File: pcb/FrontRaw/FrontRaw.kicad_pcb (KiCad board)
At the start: 2 copper layers, 54.5 x 106.4 mm, 11 parts

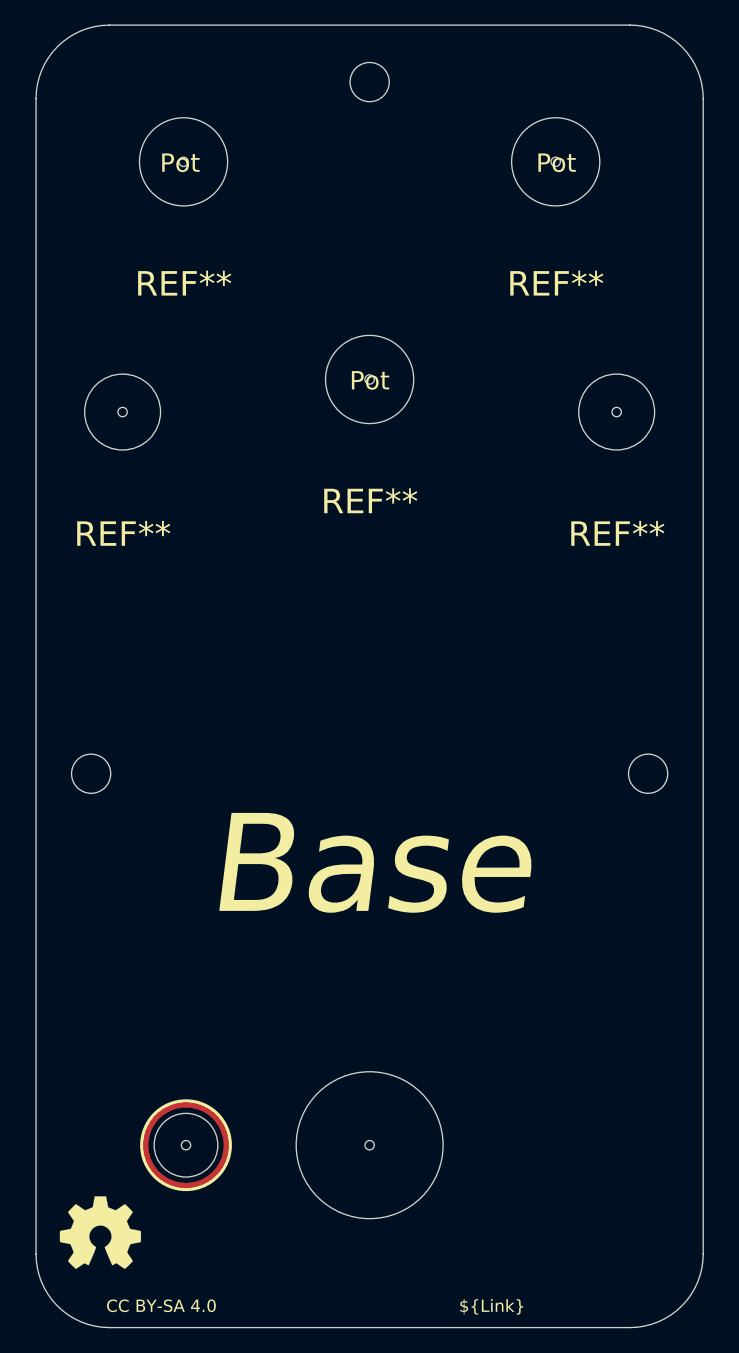
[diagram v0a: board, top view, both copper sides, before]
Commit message: [FrontRaw] Continue graphical design on frontpanel
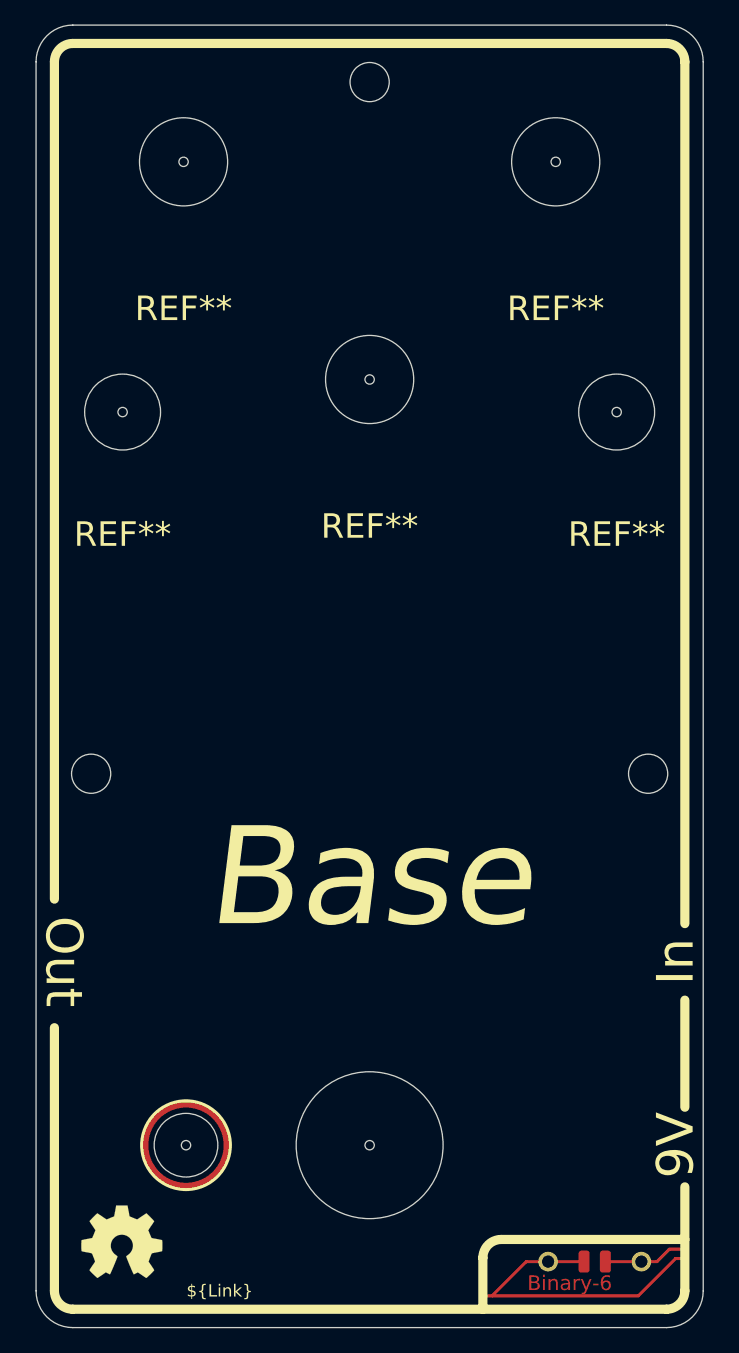
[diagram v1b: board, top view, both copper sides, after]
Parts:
- added H7: Symbol_Binary6, MeineBib:Binary_6_v0.1_tiny_silk, F.Cu at (167.9, 160.5)
- added MK6: PentThin, MeineBib:PentThin, B.Cu at (149.5, 73.4)
- moved REF** 1.90 mm to (129.2, 157.9)
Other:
- outline, holes or cut-outs redrawn
- board text added: "9V"
- board text added: "In"
- board text added: "Out"
- board text removed: "CC BY-SA 4.0"
- board text removed: "Pot"

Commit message: [FrontRaw] Add copper zones and keepout
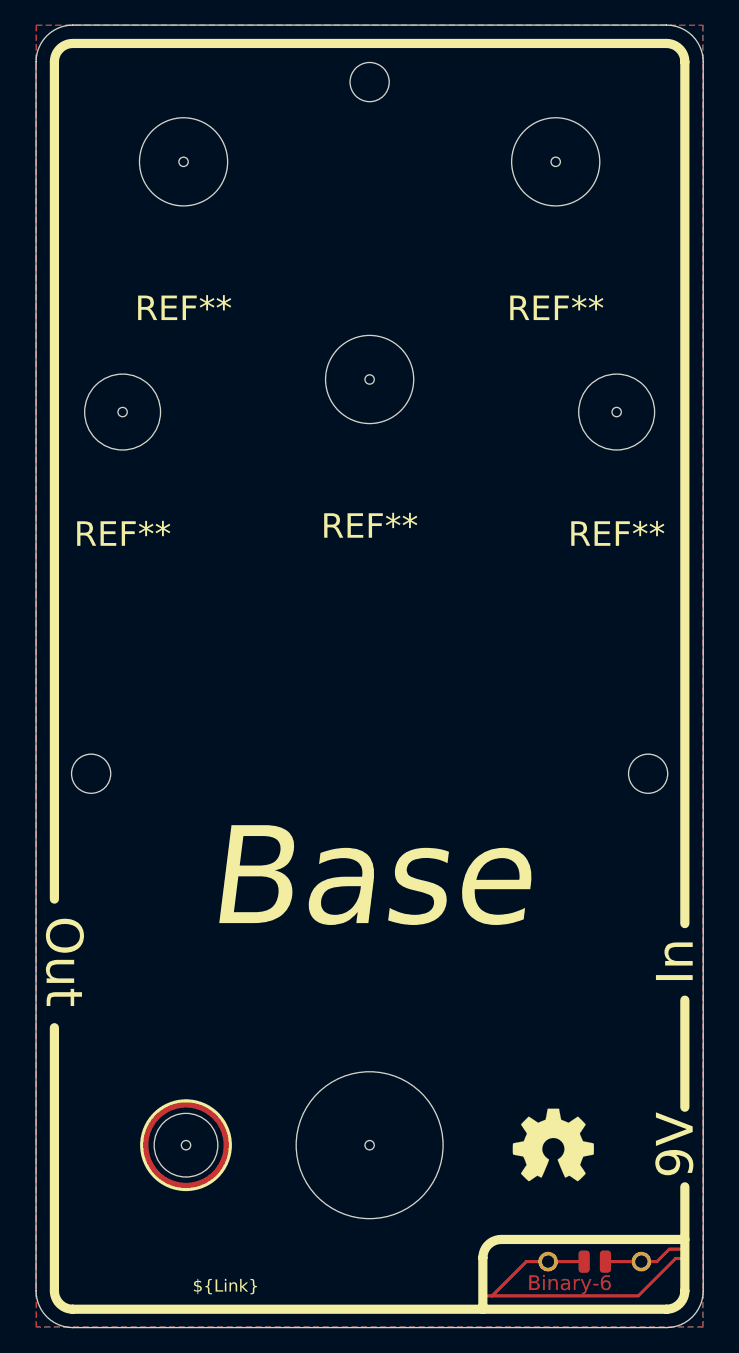
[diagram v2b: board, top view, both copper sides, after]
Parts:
- moved REF** 36.1 mm to (164.5, 150.0)
- moved MK6 0.61 mm to (149.5, 72.8)
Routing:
- added copper zone on B.Cu, net (none)
- added copper zone on F.Cu, net (none)
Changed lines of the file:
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@@
     (solder_mask_min_width 0.254)
     (aux_axis_origin 149.5 63.13)
-    (grid_origin 175.25 161.875)
+    (grid_origin 125.25 58.475)
     (pcbplotparams
       (layerselection 0x0001020_7ffffffe)
@@
   )
   (footprint "Symbol:OSHW-Symbol_6.7x6mm_SilkScreen" (layer "F.Cu")
-    (at 129.25 157.875)
+    (at 164.5 149.975)
     (descr "Open Source Hardware Symbol")
     (tags "Logo Symbol OSHW")
@@
       (effects (font (size 1 1) (thickness 0.15)))
     )
-    (pad "" np_thru_hole circle (at 0 0) (size 7.2 7.2) (drill 7.2) (layers *.Mask))
     (pad "" np_thru_hole circle (at 0 0) (size 14 14) (drill 0.762) (layers *.Mask))
+    (pad "" np_thru_hole circle (at 0 0) (size 7.2 7.2) (drill 7.2) (layers *.Mask)
+      (clearance 3.6))
   )
   (footprint "MeineBib:EigenesMountingHole_3.2mm_M3_Small" (layer "F.Cu")
@@
       (effects (font (size 1 1) (thickness 0.15)))
     )
-    (pad "" np_thru_hole circle (at 0 0) (size 6.2 6.2) (drill 6.2) (layers *.Mask))
     (pad "" np_thru_hole circle (at 0 0) (size 12 12) (drill 0.762) (layers *.Mask))
+    (pad "" np_thru_hole circle (at 0 0) (size 6.2 6.2) (drill 6.2) (layers *.Mask)
+      (clearance 3.1))
   )
   (footprint "MeineBib:Drill_ToggleSwitch_6,2mm" (layer "F.Cu")
@@
       (effects (font (size 1 1) (thickness 0.15)))
     )
-    (pad "" np_thru_hole circle (at 0 0) (size 6.2 6.2) (drill 6.2) (layers *.Mask))
     (pad "" np_thru_hole circle (at 0 0) (size 12 12) (drill 0.762) (layers *.Mask))
+    (pad "" np_thru_hole circle (at 0 0) (size 6.2 6.2) (drill 6.2) (layers *.Mask)
+      (clearance 3.1))
   )
   (footprint "MeineBib:Drill_9mmPot_7,2mm" (layer "F.Cu")
@@
       (effects (font (size 1 1) (thickness 0.15)))
     )
-    (pad "" np_thru_hole circle (at 0 0) (size 7.2 7.2) (drill 7.2) (layers *.Mask))
+    (pad "" np_thru_hole circle (at 0 0) (size 7.2 7.2) (drill 7.2) (layers *.Mask)
+      (clearance 3.6))
     (pad "" np_thru_hole circle (at 0 0) (size 14 14) (drill 0.762) (layers *.Mask))
   )
@@
       (effects (font (size 1 1) (thickness 0.15)))
     )
-    (pad "" np_thru_hole circle (at 0 0) (size 12 12) (drill 12) (layers *.Mask))
-    (pad "" np_thru_hole circle (at 0 0) (size 20 20) (drill 0.762) (layers *.Mask))
+    (pad "" np_thru_hole circle (at 0 0) (size 12 12) (drill 12) (layers *.Mask)
+      (clearance 4.2))
+    (pad "" np_thru_hole circle (at 0 0) (size 20 20) (drill 0.762) (layers *.Mask)
+      (clearance 4))
   )
   (footprint "MeineBib:EigenesMountingHole_3.2mm_M3_Small" (layer "F.Cu")
@@
     )
     (pad "" np_thru_hole circle (at 0 0) (size 14 14) (drill 0.762) (layers *.Mask))
-    (pad "" np_thru_hole circle (at 0 0) (size 7.2 7.2) (drill 7.2) (layers *.Mask))
+    (pad "" np_thru_hole circle (at 0 0) (size 7.2 7.2) (drill 7.2) (layers *.Mask)
+      (clearance 3.6))
   )
   (footprint "MeineBib:PentThin" (layer "B.Cu")
-    (at 149.5 73.375 180)
+    (at 149.450706 72.767826 180)
     (attr exclude_from_pos_files exclude_from_bom)
     (fp_text reference "MK6" (at 0 0) (layer "B.SilkS") hide
@@
     (effects (font (size 3 3) (thickness 0.6)))
   )
-  (gr_text "${Link}" (at 137.25 161.875) (layer "F.SilkS")
+  (gr_text "${Link}" (at 137.75 161.475) (layer "F.SilkS")
     (effects (font (size 1 1) (thickness 0.2)))
   )
@@
     (effects (font (size 8 8) (thickness 1.2) italic))
   )
+  (zone (net 0) (net_name "") (layers F&B.Cu) (hatch edge 0.508)
+    (connect_pads (clearance 0.508))
+    (min_thickness 0.254) (filled_areas_thickness no)
+    (fill yes (thermal_gap 0.508) (thermal_bridge_width 0.508))
+    (polygon
+      (pts
+        (xy 176.742 164.84)
+        (xy 122.266 164.84)
+        (xy 122.266 58.491)
+        (xy 176.742 58.491)
+      )
+    )
+  )
+  (zone (net 0) (net_name "") (layer "F.Cu") (hatch edge 0.508)
+    (connect_pads (clearance 0))
+    (min_thickness 0.254)
+    (keepout (tracks allowed) (vias allowed) (pads allowed ) (copperpour not_allowed) (footprints allowed))
+    (fill (thermal_gap 0.508) (thermal_bridge_width 0.508))
+    (polygon
+      (pts
+        (xy 174.89 163.015)
+        (xy 159.12 163.015)
+        (xy 159.12 158.045)
+        (xy 174.89 158.045)
+      )
+    )
+  )
   (zone (net 0) (net_name "") (layer "F.Mask") (hatch edge 0.508)
